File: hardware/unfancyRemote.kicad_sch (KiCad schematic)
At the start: 40 parts, among them J1 Arduino Analog, J2 Arduino Digital, J3 HALL1, J4 HALL2, J5 PPM, J6 VIN, J7 VBAT, J8 Motor, J9 Extra analog 1, Q1 AO3401A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

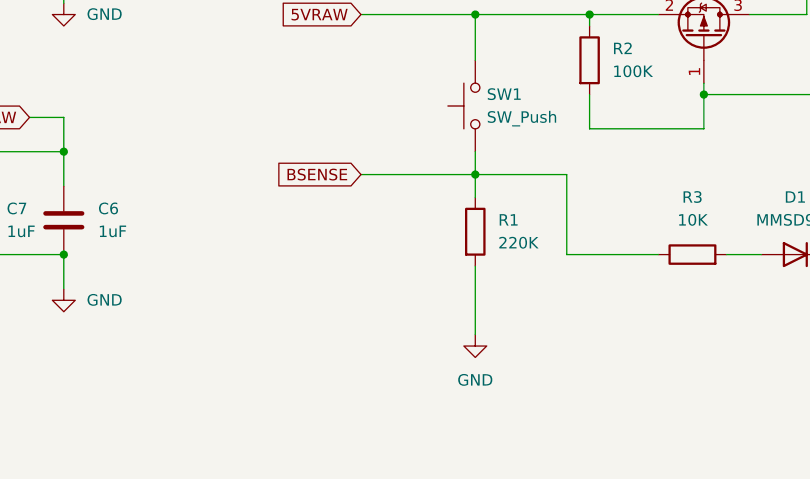
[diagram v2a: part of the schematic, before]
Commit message: Improved transmission stability
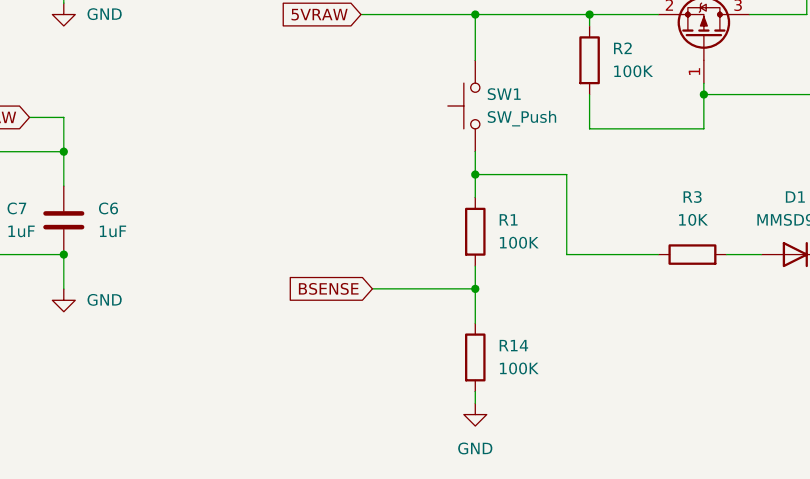
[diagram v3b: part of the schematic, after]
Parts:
- added R14: 100K, Resistor_SMD:R_0603_1608Metric, symbol Device:R
- R1: value 220K -> 100K
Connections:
- net BSENSE: now also R1.2, R14.1; no longer R1.1, R3.1, SW1.1
- net GND: now also R14.2; no longer R1.2
- new net: R1.1, R3.1, SW1.1
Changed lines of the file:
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@@
   (junction (at 43.18 83.82) (diameter 0) (color 0 0 0 0)
+  )
+  (junction (at 91.44 160.02) (diameter 0) (color 0 0 0 0)
   )
   (junction (at 134.62 156.21) (diameter 0) (color 0 0 0 0)
@@
     (stroke (width 0) (type default) (color 0 0 0 0))
   )
+  (wire (pts (xy 91.44 171.45) (xy 91.44 172.72))
+    (stroke (width 0) (type default) (color 0 0 0 0))
+  )
   (wire (pts (xy 213.36 148.59) (xy 215.9 148.59))
     (stroke (width 0) (type default) (color 0 0 0 0))
@@
     (stroke (width 0) (type default) (color 0 0 0 0))
   )
-  (wire (pts (xy 78.74 147.32) (xy 91.44 147.32))
-    (stroke (width 0) (type default) (color 0 0 0 0))
-  )
   (wire (pts (xy 156.21 127) (xy 160.02 127))
     (stroke (width 0) (type default) (color 0 0 0 0))
@@
     (stroke (width 0) (type default) (color 0 0 0 0))
   )
+  (wire (pts (xy 91.44 160.02) (xy 91.44 163.83))
+    (stroke (width 0) (type default) (color 0 0 0 0))
+  )
   (wire (pts (xy 207.01 73.66) (xy 208.28 73.66))
     (stroke (width 0) (type default) (color 0 0 0 0))
@@
     (stroke (width 0) (type default) (color 0 0 0 0))
   )
-  (wire (pts (xy 91.44 157.48) (xy 91.44 165.1))
-    (stroke (width 0) (type default) (color 0 0 0 0))
-  )
   (wire (pts (xy 175.26 82.55) (xy 177.8 82.55))
     (stroke (width 0) (type default) (color 0 0 0 0))
@@
     (stroke (width 0) (type default) (color 0 0 0 0))
   )
+  (wire (pts (xy 80.01 160.02) (xy 91.44 160.02))
+    (stroke (width 0) (type default) (color 0 0 0 0))
+  )
   (wire (pts (xy 111.76 156.21) (xy 101.6 156.21))
     (stroke (width 0) (type default) (color 0 0 0 0))
@@
   )
   (wire (pts (xy 135.89 143.51) (xy 134.62 143.51))
+    (stroke (width 0) (type default) (color 0 0 0 0))
+  )
+  (wire (pts (xy 91.44 157.48) (xy 91.44 160.02))
     (stroke (width 0) (type default) (color 0 0 0 0))
   )
@@
     )
   )
-  (global_label "BSENSE" (shape input) (at 78.74 147.32 180) (fields_autoplaced)
+  (global_label "BSENSE" (shape input) (at 80.01 160.02 180) (fields_autoplaced)
     (effects (font (size 1.27 1.27)) (justify right))
-    (property "Intersheet References" "${INTERSHEET_REFS}" (id 0) (at 69.0093 147.2406 0)
+    (property "Intersheet References" "${INTERSHEET_REFS}" (id 0) (at 70.2793 159.9406 0)
       (effects (font (size 1.27 1.27)) (justify right) hide)
     )
@@
     (pin "9")
   )
+  (symbol (lib_id "Device:R") (at 91.44 167.64 0) (unit 1)
+    (in_bom yes) (on_board yes) (fields_autoplaced)
+    (property "Reference" "R14" (id 0) (at 93.98 166.3699 0)
+      (effects (font (size 1.27 1.27)) (justify left))
+    )
+    (property "Value" "100K" (id 1) (at 93.98 168.9099 0)
+      (effects (font (size 1.27 1.27)) (justify left))
+    )
+    (property "Footprint" "Resistor_SMD:R_0603_1608Metric" (id 2) (at 89.662 167.64 90)
+      (effects (font (size 1.27 1.27)) hide)
+    )
+    (property "Datasheet" "~" (id 3) (at 91.44 167.64 0)
+      (effects (font (size 1.27 1.27)) hide)
+    )
+    (property "LCSC" "C22961" (id 4) (at 91.44 167.64 0)
+      (effects (font (size 1.27 1.27)) hide)
+    )
+    (pin "1")
+    (pin "2")
+  )
   (symbol (lib_id "power:GND") (at 200.66 125.73 270) (unit 1)
     (in_bom yes) (on_board yes) (fields_autoplaced)
@@
       (effects (font (size 1.27 1.27)) (justify left))
     )
-    (property "Value" "220K" (id 1) (at 93.98 154.9399 0)
+    (property "Value" "100K" (id 1) (at 93.98 154.9399 0)
       (effects (font (size 1.27 1.27)) (justify left))
     )
@@
     (pin "2")
   )
-  (symbol (lib_id "power:GND") (at 91.44 165.1 0) (unit 1)
-    (in_bom yes) (on_board yes) (fields_autoplaced)
-    (property "Reference" "#PWR0116" (id 0) (at 91.44 171.45 0)
-      (effects (font (size 1.27 1.27)) hide)
-    )
-    (property "Value" "GND" (id 1) (at 91.44 170.18 0))
-    (property "Footprint" "" (id 2) (at 91.44 165.1 0)
-      (effects (font (size 1.27 1.27)) hide)
-    )
-    (property "Datasheet" "" (id 3) (at 91.44 165.1 0)
+  (symbol (lib_id "power:GND") (at 91.44 172.72 0) (unit 1)
+    (in_bom yes) (on_board yes) (fields_autoplaced)
+    (property "Reference" "#PWR0116" (id 0) (at 91.44 179.07 0)
+      (effects (font (size 1.27 1.27)) hide)
+    )
+    (property "Value" "GND" (id 1) (at 91.44 177.8 0))
+    (property "Footprint" "" (id 2) (at 91.44 172.72 0)
+      (effects (font (size 1.27 1.27)) hide)
+    )
+    (property "Datasheet" "" (id 3) (at 91.44 172.72 0)
       (effects (font (size 1.27 1.27)) hide)
     )
@@
     )
     (path "/992bfab4-6c3b-4d75-b8a7-dddbe50318ad"
-      (reference "R1") (unit 1) (value "220K") (footprint "Resistor_SMD:R_0603_1608Metric")
+      (reference "R1") (unit 1) (value "100K") (footprint "Resistor_SMD:R_0603_1608Metric")
     )
     (path "/8ee26396-cfa7-4786-be63-57d651d4959b"
@@
       (reference "R13") (unit 1) (value "6.8K") (footprint "Resistor_SMD:R_0603_1608Metric")
     )
+    (path "/381e66ec-dddb-4e4c-9abe-e5309b541128"
+      (reference "R14") (unit 1) (value "100K") (footprint "Resistor_SMD:R_0603_1608Metric")
+    )
     (path "/8e875e7b-f435-48fe-904e-cd96af2470b5"

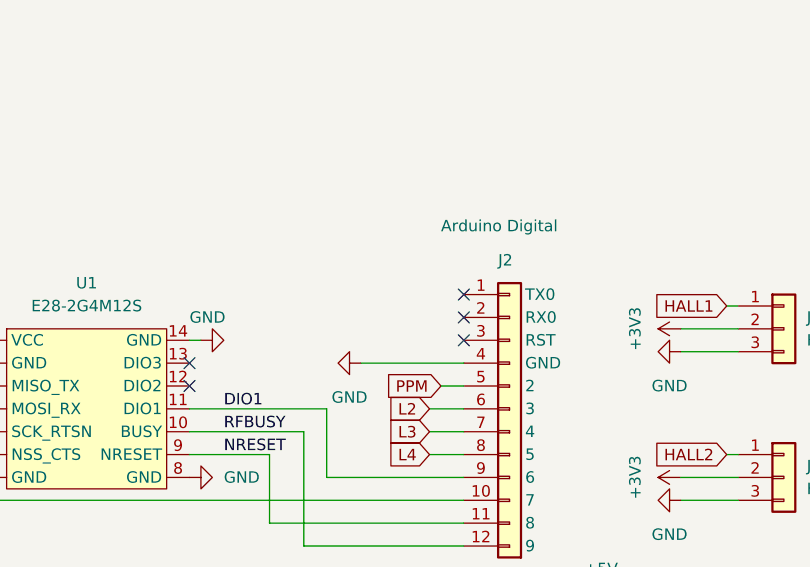
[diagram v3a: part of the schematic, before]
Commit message: PCB improvements, round version, cal procedure
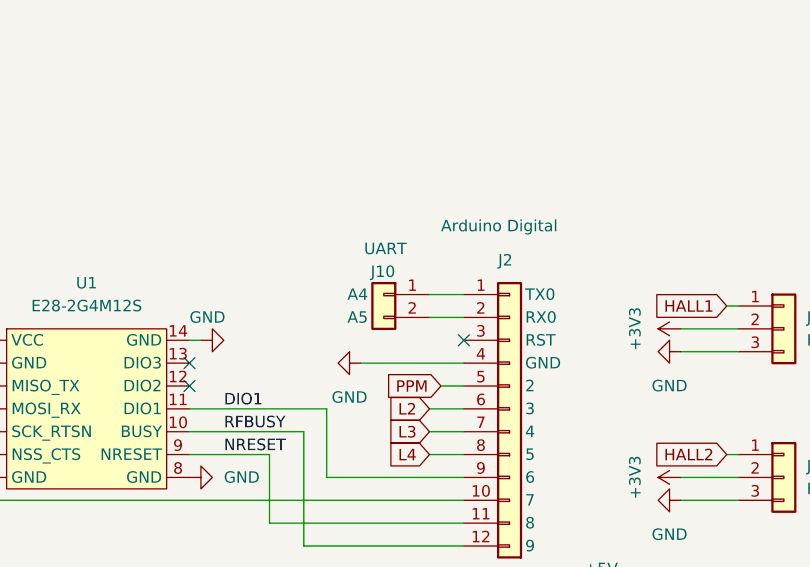
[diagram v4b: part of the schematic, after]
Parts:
- added J10: UART, unfancyRemote_components:SolderWirePad_1x02_SMD_1x2mm, symbol unfancyRemote_components:Extra_analog_1
- J3, J4, J5: footprint Connector_JST:JST_PH_B3B-PH-K_1x03_P2.00mm_Vertical -> unfancyRemote_components:SolderWirePad_1x03_SMD_1x2mm
- J6: footprint Connector_JST:JST_PH_B2B-PH-K_1x02_P2.00mm_Vertical -> unfancyRemote_components:SolderWirePad_1x02_SMD_1x2mm
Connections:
- net at J2.1 (TX0): now also J10.1 (A4)
- net at J2.2 (RX0): now also J10.2 (A5)
- no-connect marks 7 -> 5
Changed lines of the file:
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@@
   (no_connect (at 147.32 82.55))
   (no_connect (at 147.32 80.01))
-  (no_connect (at 177.8 72.39))
   (no_connect (at 177.8 77.47))
-  (no_connect (at 177.8 74.93))
   (no_connect (at 93.98 77.47))
   (no_connect (at 242.57 76.2))
@@
     (stroke (width 0) (type default) (color 0 0 0 0))
   )
+  (wire (pts (xy 173.99 72.39) (xy 177.8 72.39))
+    (stroke (width 0) (type default) (color 0 0 0 0))
+  )
   (wire (pts (xy 175.26 82.55) (xy 177.8 82.55))
     (stroke (width 0) (type default) (color 0 0 0 0))
@@
   )
   (wire (pts (xy 93.98 74.93) (xy 104.14 74.93))
+    (stroke (width 0) (type default) (color 0 0 0 0))
+  )
+  (wire (pts (xy 173.99 74.93) (xy 177.8 74.93))
     (stroke (width 0) (type default) (color 0 0 0 0))
   )
@@
       (effects (font (size 1.27 1.27)) (justify left))
     )
-    (property "Footprint" "Connector_JST:JST_PH_B3B-PH-K_1x03_P2.00mm_Vertical" (id 2) (at 213.36 107.95 0)
+    (property "Footprint" "unfancyRemote_components:SolderWirePad_1x03_SMD_1x2mm" (id 2) (at 213.36 107.95 0)
       (effects (font (size 1.27 1.27)) hide)
     )
@@
       (effects (font (size 1.27 1.27)) (justify left))
     )
-    (property "Footprint" "Connector_JST:JST_PH_B2B-PH-K_1x02_P2.00mm_Vertical" (id 2) (at 76.2 115.57 0)
+    (property "Footprint" "unfancyRemote_components:SolderWirePad_1x02_SMD_1x2mm" (id 2) (at 76.2 115.57 0)
       (effects (font (size 1.27 1.27)) hide)
     )
@@
       (effects (font (size 1.27 1.27)) (justify left))
     )
-    (property "Footprint" "Connector_JST:JST_PH_B3B-PH-K_1x03_P2.00mm_Vertical" (id 2) (at 213.36 92.71 0)
+    (property "Footprint" "unfancyRemote_components:SolderWirePad_1x03_SMD_1x2mm" (id 2) (at 213.36 92.71 0)
       (effects (font (size 1.27 1.27)) hide)
     )
@@
       (effects (font (size 1.27 1.27)) (justify left))
     )
-    (property "Footprint" "Connector_JST:JST_PH_B3B-PH-K_1x03_P2.00mm_Vertical" (id 2) (at 213.36 76.2 0)
+    (property "Footprint" "unfancyRemote_components:SolderWirePad_1x03_SMD_1x2mm" (id 2) (at 213.36 76.2 0)
       (effects (font (size 1.27 1.27)) hide)
     )
@@
     (pin "1")
   )
+  (symbol (lib_id "unfancyRemote_components:Extra_analog_1") (at 168.91 72.39 0) (mirror y) (unit 1)
+    (in_bom yes) (on_board yes)
+    (property "Reference" "J10" (id 0) (at 170.18 69.85 0)
+      (effects (font (size 1.27 1.27)) (justify left))
+    )
+    (property "Value" "UART" (id 1) (at 171.45 67.31 0)
+      (effects (font (size 1.27 1.27)) (justify left))
+    )
+    (property "Footprint" "unfancyRemote_components:SolderWirePad_1x02_SMD_1x2mm" (id 2) (at 168.91 72.39 0)
+      (effects (font (size 1.27 1.27)) hide)
+    )
+    (property "Datasheet" "~" (id 3) (at 168.91 72.39 0)
+      (effects (font (size 1.27 1.27)) hide)
+    )
+    (pin "1")
+    (pin "2")
+  )
   (symbol (lib_id "power:GND") (at 104.14 74.93 90) (unit 1)
     (in_bom yes) (on_board yes) (fields_autoplaced)
@@
     )
     (path "/a89a63aa-b5bb-4c83-98b3-35f885559ff8"
-      (reference "J3") (unit 1) (value "HALL1") (footprint "Connector_JST:JST_PH_B3B-PH-K_1x03_P2.00mm_Vertical")
+      (reference "J3") (unit 1) (value "HALL1") (footprint "unfancyRemote_components:SolderWirePad_1x03_SMD_1x2mm")
     )
     (path "/51893d48-1045-4db6-8142-e463331ac0f8"
-      (reference "J4") (unit 1) (value "HALL2") (footprint "Connector_JST:JST_PH_B3B-PH-K_1x03_P2.00mm_Vertical")
+      (reference "J4") (unit 1) (value "HALL2") (footprint "unfancyRemote_components:SolderWirePad_1x03_SMD_1x2mm")
     )
     (path "/13f1adfa-4c7a-4303-a883-75e9ac894762"
-      (reference "J5") (unit 1) (value "PPM") (footprint "Connector_JST:JST_PH_B3B-PH-K_1x03_P2.00mm_Vertical")
+      (reference "J5") (unit 1) (value "PPM") (footprint "unfancyRemote_components:SolderWirePad_1x03_SMD_1x2mm")
     )
     (path "/200c1ca0-4bb9-4f6c-a01d-e8e5bdd9d6b6"
-      (reference "J6") (unit 1) (value "VIN") (footprint "Connector_JST:JST_PH_B2B-PH-K_1x02_P2.00mm_Vertical")
+      (reference "J6") (unit 1) (value "VIN") (footprint "unfancyRemote_components:SolderWirePad_1x02_SMD_1x2mm")
     )
     (path "/e1977d8d-9dff-44d4-a267-0aad5bbad045"
@@
       (reference "J9") (unit 1) (value "Extra analog 1") (footprint "Connector_PinSocket_2.54mm:PinSocket_1x02_P2.54mm_Vertical")
     )
+    (path "/f01717ce-5ea2-40bb-b345-2f1eb154ce2d"
+      (reference "J10") (unit 1) (value "UART") (footprint "unfancyRemote_components:SolderWirePad_1x02_SMD_1x2mm")
+    )
     (path "/0b2234c3-2d14-4061-8885-76abbdce278a"
